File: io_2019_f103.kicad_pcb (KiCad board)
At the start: 2 copper layers, 69.5 x 90.2 mm, 49 parts, among them J1 Con_Tirette, J10 Con_EV, J11 Con_EV, J12 Con_EV, J13 Con_EV, J2 Conn_01x04, J3 Conn_01x20_Female, J4 Alim logique, J5 Conn_01x20_Female, J6 Liaison serie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

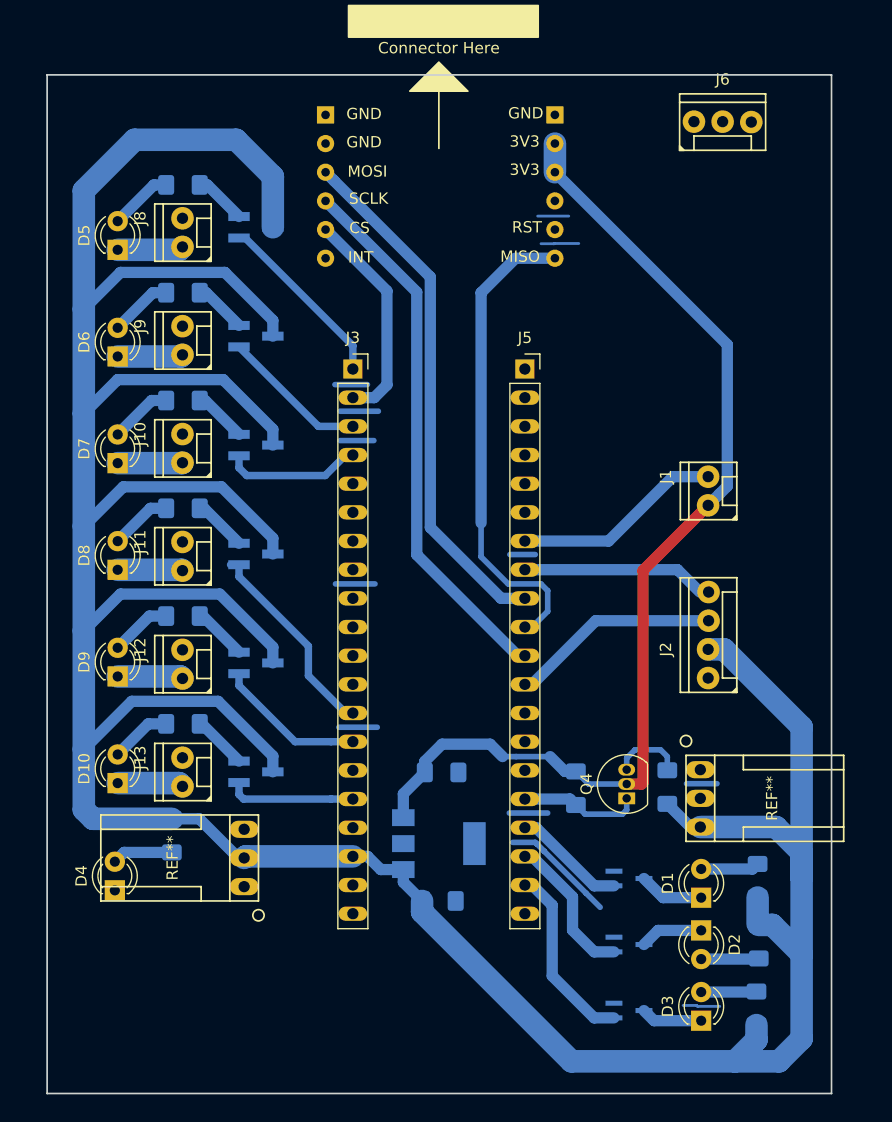
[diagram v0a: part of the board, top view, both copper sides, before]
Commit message: Add drill hole, and version text
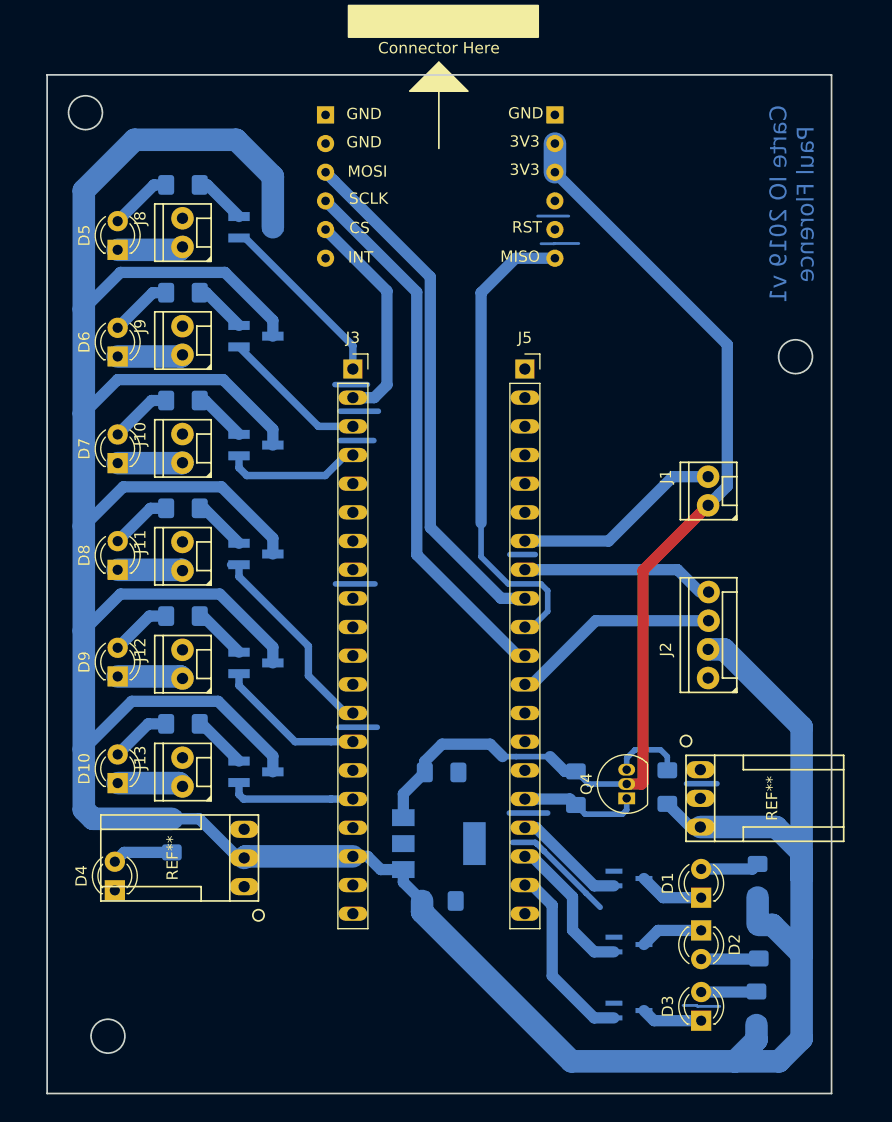
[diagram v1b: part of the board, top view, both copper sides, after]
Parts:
- removed J6: Liaison serie, @Robot:HE14-3-straight
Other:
- outline, holes or cut-outs redrawn
- board text added: "Carte IO 2019 v1 Paul Florence"

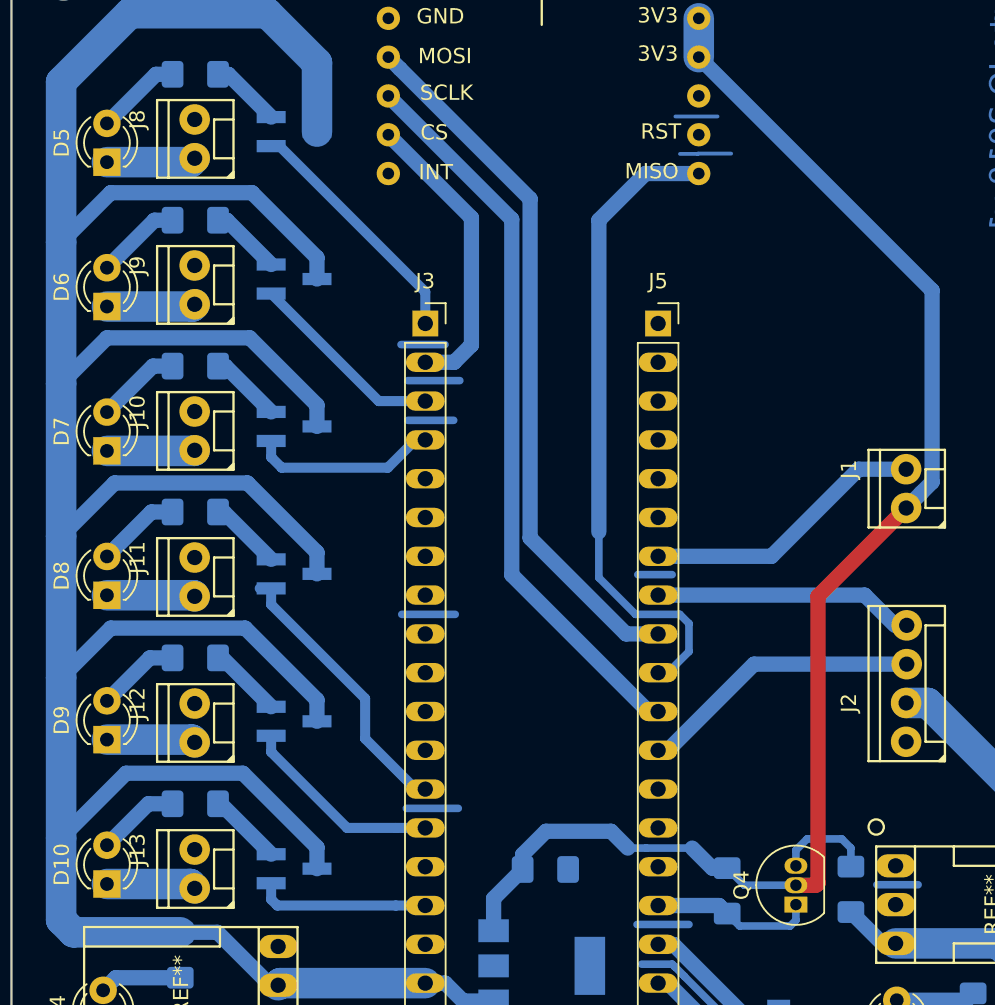
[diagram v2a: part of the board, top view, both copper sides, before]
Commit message: Modification driver electrovannes
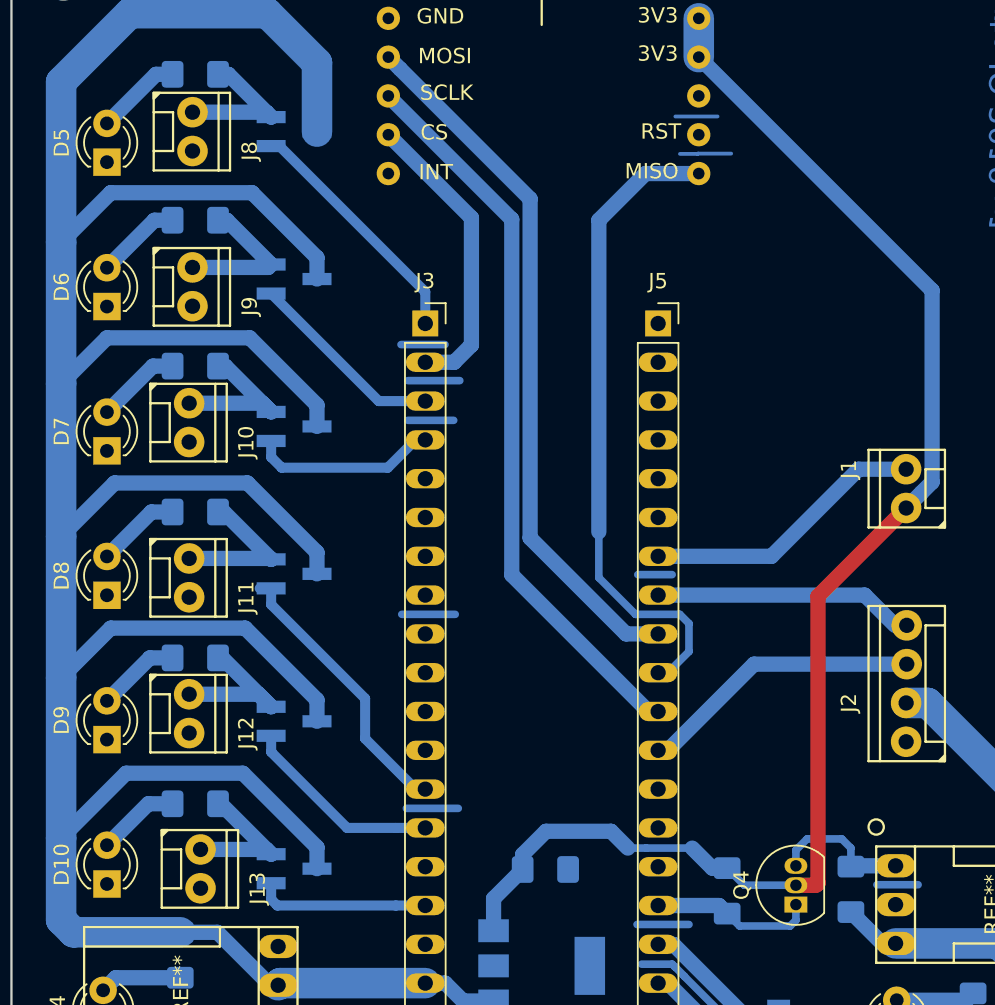
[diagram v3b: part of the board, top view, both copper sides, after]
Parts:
- Q10, Q5, Q6, Q7, Q8, Q9: value Q_NMOS_GSD -> NDS351AN
- moved J13 3.15 mm to (102.9, 113.0), turned to 270 degrees
- moved J9 2.99 mm to (102.3, 74.9), turned to 270 degrees
- moved J11 2.83 mm to (102.1, 94.0), turned to 270 degrees
- moved J8 2.46 mm to (102.3, 64.8), turned to 270 degrees
- moved J10 2.29 mm to (102.1, 83.8), turned to 270 degrees
- moved J12 2.24 mm to (102.1, 102.9), turned to 270 degrees
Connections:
- D10 pad 1: Net-(D10-Pad1) -> GND
- D5 pad 1: Net-(D5-Pad1) -> GND
- D6 pad 1: Net-(D6-Pad1) -> GND
- D7 pad 1: Net-(D7-Pad1) -> GND
- D8 pad 1: Net-(D8-Pad1) -> GND
- D9 pad 1: Net-(D9-Pad1) -> GND
- J10 pad 1: Net-(D7-Pad1) -> Net-(J10-Pad1)
- J11 pad 1: Net-(D8-Pad1) -> Net-(J11-Pad1)
- J12 pad 1: Net-(D9-Pad1) -> Net-(J12-Pad1)
- J13 pad 1: Net-(D10-Pad1) -> Net-(J13-Pad1)
- J8 pad 1: Net-(D5-Pad1) -> Net-(J8-Pad1)
- J9 pad 1: Net-(D6-Pad1) -> Net-(J9-Pad1)
- Q10 pad 2: Net-(Q10-Pad2) -> Net-(J13-Pad1)
- Q5 pad 2: Net-(Q5-Pad2) -> Net-(J8-Pad1)
- Q6 pad 2: Net-(Q6-Pad2) -> Net-(J9-Pad1)
- Q7 pad 2: Net-(Q7-Pad2) -> Net-(J10-Pad1)
- Q8 pad 2: Net-(Q8-Pad2) -> Net-(J11-Pad1)
- Q9 pad 2: Net-(Q9-Pad2) -> Net-(J12-Pad1)
- R10 pad 2: Net-(Q8-Pad2) -> Net-(J11-Pad1)
- R11 pad 2: Net-(Q9-Pad2) -> Net-(J12-Pad1)
- R12 pad 2: Net-(Q10-Pad2) -> Net-(J13-Pad1)
- R7 pad 2: Net-(Q5-Pad2) -> Net-(J8-Pad1)
- R8 pad 2: Net-(Q6-Pad2) -> Net-(J9-Pad1)
- R9 pad 2: Net-(Q7-Pad2) -> Net-(J10-Pad1)
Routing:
- net Net-(J12-Pad1): track 0.00 -> 10.5 mm
- net Net-(J10-Pad1): track 0.00 -> 10.3 mm
- net Net-(J11-Pad1): track 0.00 -> 10.2 mm
- net Net-(J8-Pad1): track 0.00 -> 9.92 mm
- net Net-(J9-Pad1): track 0.00 -> 9.91 mm
- net Net-(J13-Pad1): track 0.00 -> 9.60 mm
- net Net-(D10-Pad1): track 5.86 -> 0.00 mm
- net Net-(D5-Pad1): track 5.85 -> 0.00 mm
- net Net-(D9-Pad1): track 5.82 -> 0.00 mm
- net Net-(D6-Pad1): track 5.80 -> 0.00 mm
- net Net-(D8-Pad1): track 5.77 -> 0.00 mm
- net Net-(D7-Pad1): track 5.76 -> 0.00 mm
- net Net-(Q10-Pad2): track 4.85 -> 0.00 mm
- net Net-(Q9-Pad2): track 4.80 -> 0.00 mm
- net Net-(Q8-Pad2): track 4.76 -> 0.00 mm
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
